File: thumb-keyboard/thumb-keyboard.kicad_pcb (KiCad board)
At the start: 2 copper layers, 120 x 60 mm, 128 parts, among them J1 Conn_01x02_Socket, U1 nice_nano

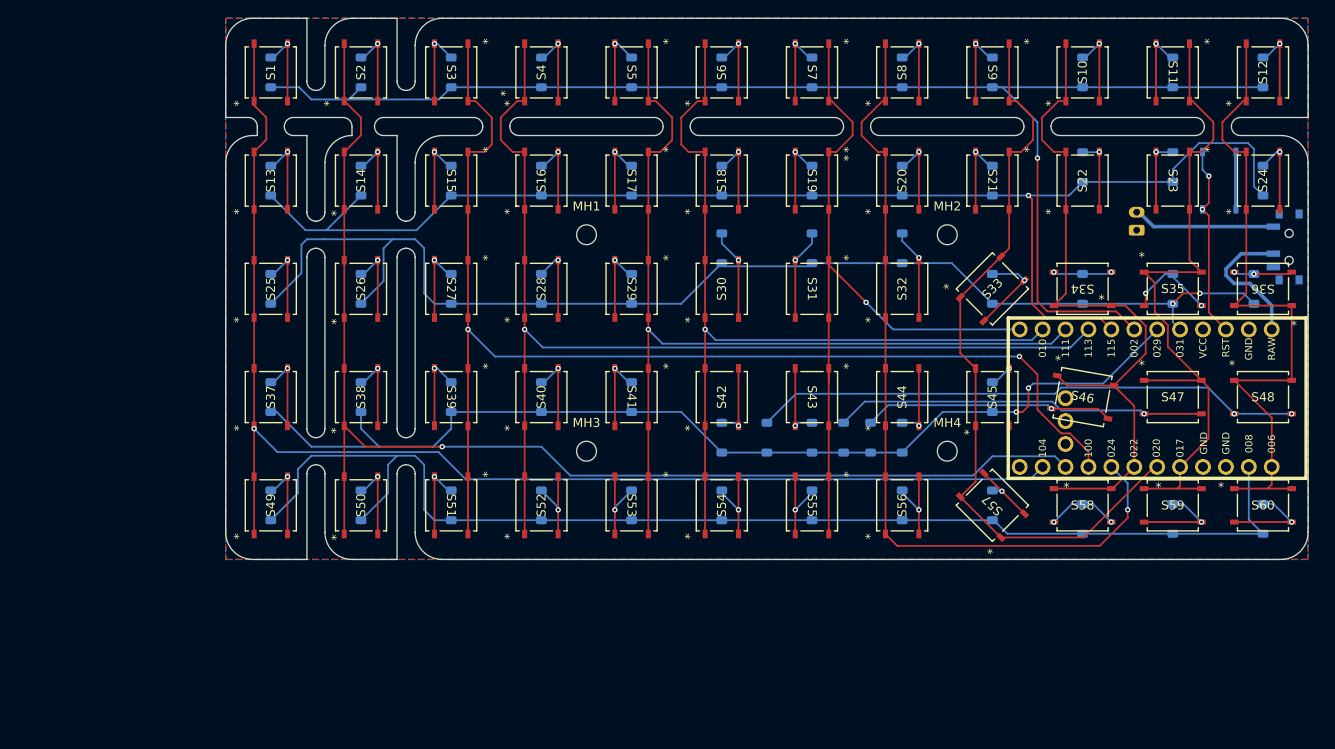
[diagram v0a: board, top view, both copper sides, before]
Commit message: going to try reducing the slot diam
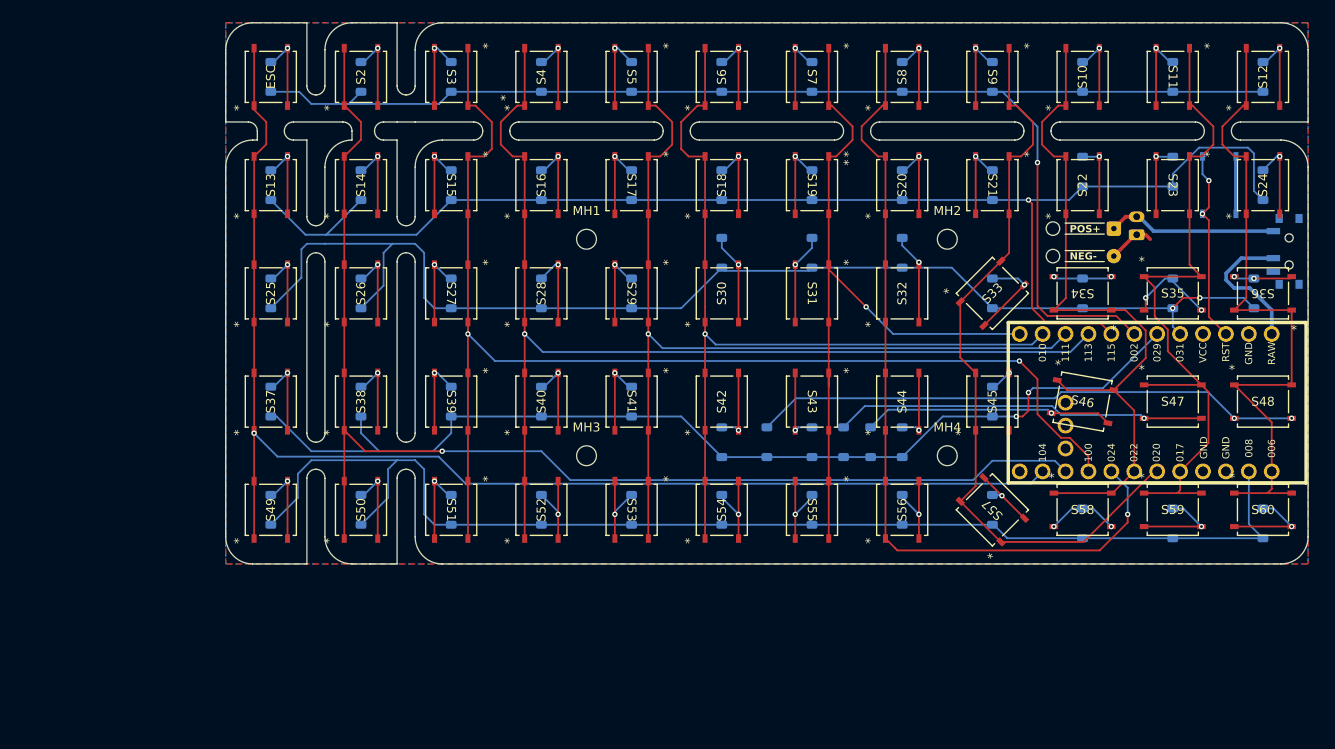
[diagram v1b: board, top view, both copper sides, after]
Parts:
- added GND - POS: SolderWire-0.1sqmm_1x02_P3.6mm_D0.4mm_OD1mm_Relief, Connector_Wire:SolderWire-0.1sqmm_1x02_P3.6mm_D0.4mm_OD1mm_Relief, F.Cu at (178.5, 70.6)
- S1: value PTS526 SK15 SMTR2 LFS -> ESC
- moved D1 0.50 mm to (85.0, 54.0)
- moved D10 0.50 mm to (175.0, 54.0)
- moved D11 0.50 mm to (185.0, 54.0)
- moved D12 0.50 mm to (195.0, 54.0)
- moved D13 0.50 mm to (85.0, 66.0)
- moved D14 0.50 mm to (95.0, 66.0)
- moved D15 0.50 mm to (105.0, 66.0)
- moved D16 0.50 mm to (115.0, 66.0)
- moved D17 0.50 mm to (125.0, 66.0)
- moved D18 0.50 mm to (135.0, 66.0)
- moved D19 0.50 mm to (145.0, 66.0)
- moved D2 0.50 mm to (95.0, 54.0)
- moved D20 0.50 mm to (155.0, 66.0)
- moved D21 0.50 mm to (165.0, 66.0)
- moved D22 0.50 mm to (175.0, 64.5)
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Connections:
- S62 pad SH1: /GND -> (no net)
- S62 pad SH2: /GND -> (no net)
- S62 pad SH3: /GND -> (no net)
- S62 pad SH4: /GND -> (no net)
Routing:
- net /GND: track 6.36 -> 11.6 mm
- net /BATP: track 15.8 -> 18.9 mm
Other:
- board text added: "NEG-"
- board text added: "POS+"

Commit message: Added ws2812b leds to thumb keyboard. they may be too tall. I may have to switch to the 222AMVBAR tactile switches and space everything out like a centimeter more. that would be a lot of work but would open up for other types of switches
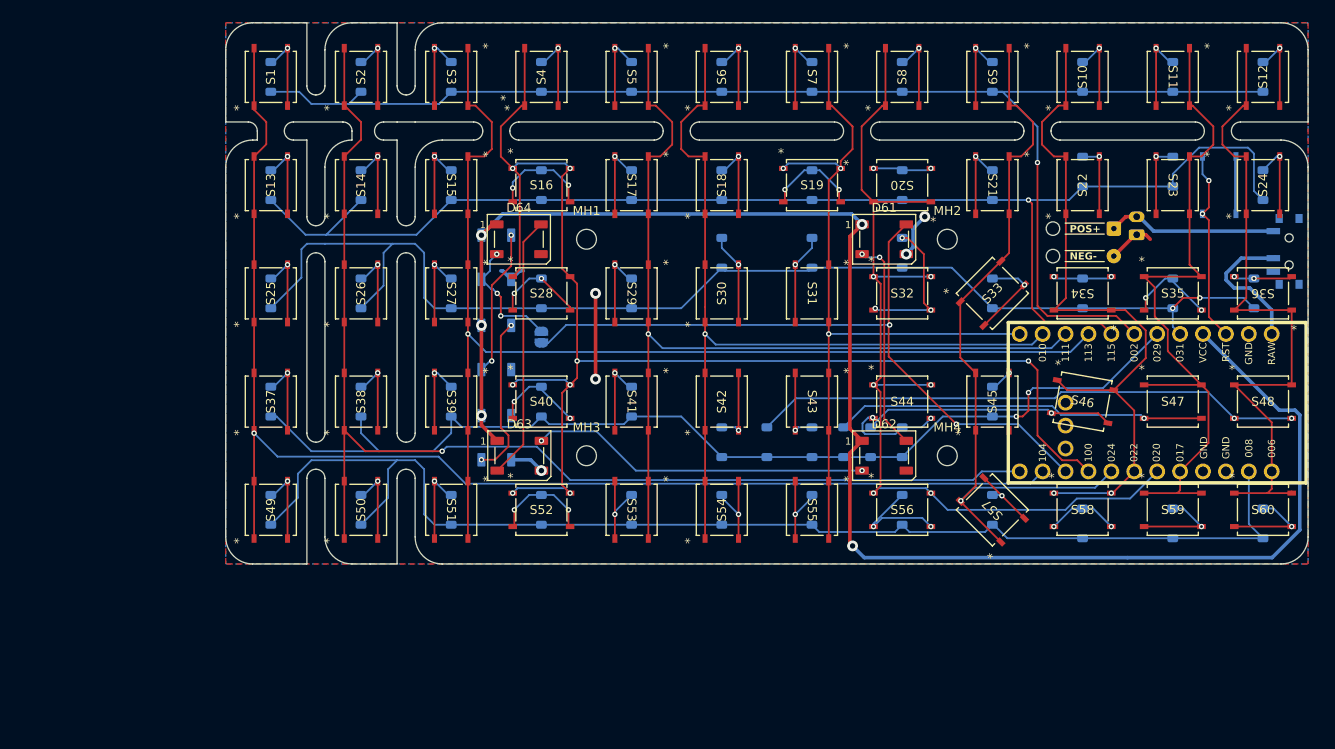
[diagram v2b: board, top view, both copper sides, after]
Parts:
- added D61: WS2812B, LED_SMD:LED_WS2812B_PLCC4_5.0x5.0mm_P3.2mm, F.Cu at (153.0, 72.0)
- added D62: WS2812B, LED_SMD:LED_WS2812B_PLCC4_5.0x5.0mm_P3.2mm, F.Cu at (153.0, 96.0)
- added D63: WS2812B, LED_SMD:LED_WS2812B_PLCC4_5.0x5.0mm_P3.2mm, F.Cu at (112.5, 96.0)
- added D64: WS2812B, LED_SMD:LED_WS2812B_PLCC4_5.0x5.0mm_P3.2mm, F.Cu at (112.5, 72.0)
- added D65: WS2812B, LED_SMD:LED_WS2812B_PLCC4_5.0x5.0mm_P3.2mm, B.Cu at (110.0, 74.0)
- added D66: WS2812B, LED_SMD:LED_WS2812B_PLCC4_5.0x5.0mm_P3.2mm, B.Cu at (110.0, 84.0)
- added D67: WS2812B, LED_SMD:LED_WS2812B_PLCC4_5.0x5.0mm_P3.2mm, B.Cu at (110.0, 94.0)
- added JumpIfNoFrontLED: SolderJumper-2_P1.3mm_Open_RoundedPad1.0x1.5mm, Jumper:SolderJumper-2_P1.3mm_Open_RoundedPad1.0x1.5mm, B.Cu at (115.0, 82.8)
- S1, S10, S11, S12, S13, S14, S15, S16, S17, S18, S19, S2, S20, S21, S22, S23, S24, S25, S26, S27, S28, S29, S3, S30, S31, S32, S33, S34, S35, S36, S37, S38, S39, S4, S40, S41, S42, S43, S44, S45, S46, S47, S48, S49, S5, S50, S51, S52, S53, S54, S55, S56, S57, S58, S59, S6, S60, S61, S7, S8, S9: footprint footprints:SMT_FS -> lowproswitch:SMT_FS
- turned S16 to 0 degrees
- turned S19 to 0 degrees
- turned S20 to 180 degrees
- turned S28 to 0 degrees
- turned S32 to 0 degrees
- turned S40 to 0 degrees
- turned S44 to 0 degrees
- turned S52 to 0 degrees
- turned S56 to 0 degrees
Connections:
- net Net-(D1-A) renamed /C0R0D
- U1 pad 10: /COL1 -> /RGBDIN
- U1 pad 12: unconnected-(U1-P1.06-Pad12) -> /COL1
- U1 pad 16: /COL3 -> /COL2
- U1 pad 21: unconnected-(U1-VCC-Pad21) -> /VCC
- U1 pad 6: /COL8 -> /COL7
- U1 pad 8: /COL7 -> /COL8
- U1 pad 9: /COL2 -> /COL3
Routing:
- net /VCC: track 0.00 -> 185.6 mm, vias 0 -> 5
- net /RGBDIN: track 0.00 -> 79.8 mm, vias 0 -> 2
- net Net-(D62-DOUT): track 0.00 -> 37.8 mm, vias 0 -> 2
- net /COL3: track 122.0 -> 152.4 mm, vias 1 -> 8
- net Net-(D63-DOUT): track 0.00 -> 29.3 mm
- net Net-(D61-DOUT): track 0.00 -> 23.7 mm, vias 0 -> 2
- net /GND: track 11.6 -> 33.2 mm, vias 0 -> 5
- net Net-(D66-DOUT): track 0.00 -> 17.9 mm, vias 0 -> 2
- net Net-(D65-DOUT): track 0.00 -> 16.4 mm, vias 0 -> 2
- net Net-(D64-DOUT): track 0.00 -> 13.8 mm, vias 0 -> 3
- net /COL7: track 92.3 -> 106.0 mm, vias 1 -> 6
- net /COL2: track 136.5 -> 128.6 mm, vias 2 -> 1
- net Net-(D32-A): track 9.83 -> 15.9 mm, vias 1 -> 3
- net /COL1: track 139.5 -> 133.9 mm
- net Net-(D56-A): track 9.28 -> 12.3 mm, vias 1 -> 2
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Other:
- board text added: "301230 battery"

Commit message: working on different switches. last commit before adding the B3F-1000 switch option and extending the x gap from 10 - 12 mm
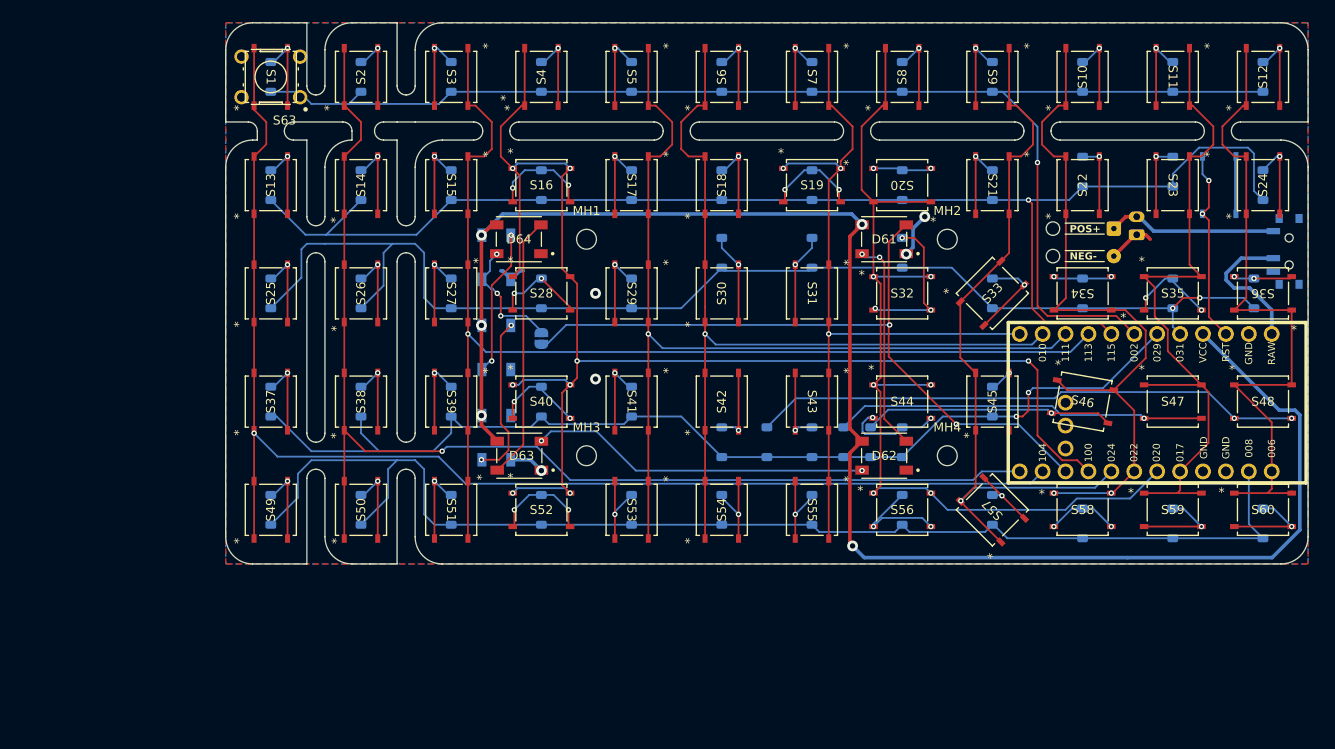
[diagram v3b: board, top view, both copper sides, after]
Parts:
- added S63: B3F-1000, B3F_1000:SW_B3F-1000, F.Cu at (85.0, 54.0)
- D61, D62, D63, D64, D65, D66, D67: footprint LED_SMD:LED_WS2812B_PLCC4_5.0x5.0mm_P3.2mm -> 1655:LED_1655
- moved JumpIfNoFrontLED 0.15 mm to (115.0, 83.0)
- turned D61 to 180 degrees
- turned D62 to 180 degrees
- turned D63 to 180 degrees
- turned D64 to 180 degrees
- turned D65 to 90 degrees
- turned D66 to 90 degrees
- turned D67 to 90 degrees
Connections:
- D61 pad 1: /VCC -> /GND
- D61 pad 2: Net-(D61-DOUT) -> /RGBDIN
- D61 pad 3: /GND -> /VCC
- D61 pad 4: /RGBDIN -> Net-(D61-DOUT)
- D62 pad 1: /VCC -> /GND
- D62 pad 2: Net-(D62-DOUT) -> Net-(D61-DOUT)
- D62 pad 3: /GND -> /VCC
- D62 pad 4: Net-(D61-DOUT) -> Net-(D62-DOUT)
- D63 pad 1: /VCC -> /GND
- D63 pad 2: Net-(D63-DOUT) -> Net-(D62-DOUT)
- D63 pad 3: /GND -> /VCC
- D63 pad 4: Net-(D62-DOUT) -> Net-(D63-DOUT)
- D64 pad 1: /VCC -> /GND
- D64 pad 2: Net-(D64-DOUT) -> Net-(D63-DOUT)
- D64 pad 3: /GND -> /VCC
- D64 pad 4: Net-(D63-DOUT) -> Net-(D64-DOUT)
- D65 pad 1: /VCC -> /GND
- D65 pad 2: Net-(D65-DOUT) -> Net-(D64-DOUT)
- D65 pad 3: /GND -> /VCC
- D65 pad 4: Net-(D64-DOUT) -> Net-(D65-DOUT)
- D66 pad 1: /VCC -> /GND
- D66 pad 2: Net-(D66-DOUT) -> Net-(D65-DOUT)
- D66 pad 3: /GND -> /VCC
- D66 pad 4: Net-(D65-DOUT) -> Net-(D66-DOUT)
- D67 pad 1: /VCC -> /GND
- D67 pad 2: unconnected-(D67-DOUT-Pad2) -> Net-(D66-DOUT)
- D67 pad 3: /GND -> /VCC
- D67 pad 4: Net-(D66-DOUT) -> unconnected-(D67-DOUT-Pad4)
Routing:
- net /GND: track 33.2 -> 23.7 mm

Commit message: first commit after change to branch with optional B3F-1000 switches. footprint is going to be 144x60
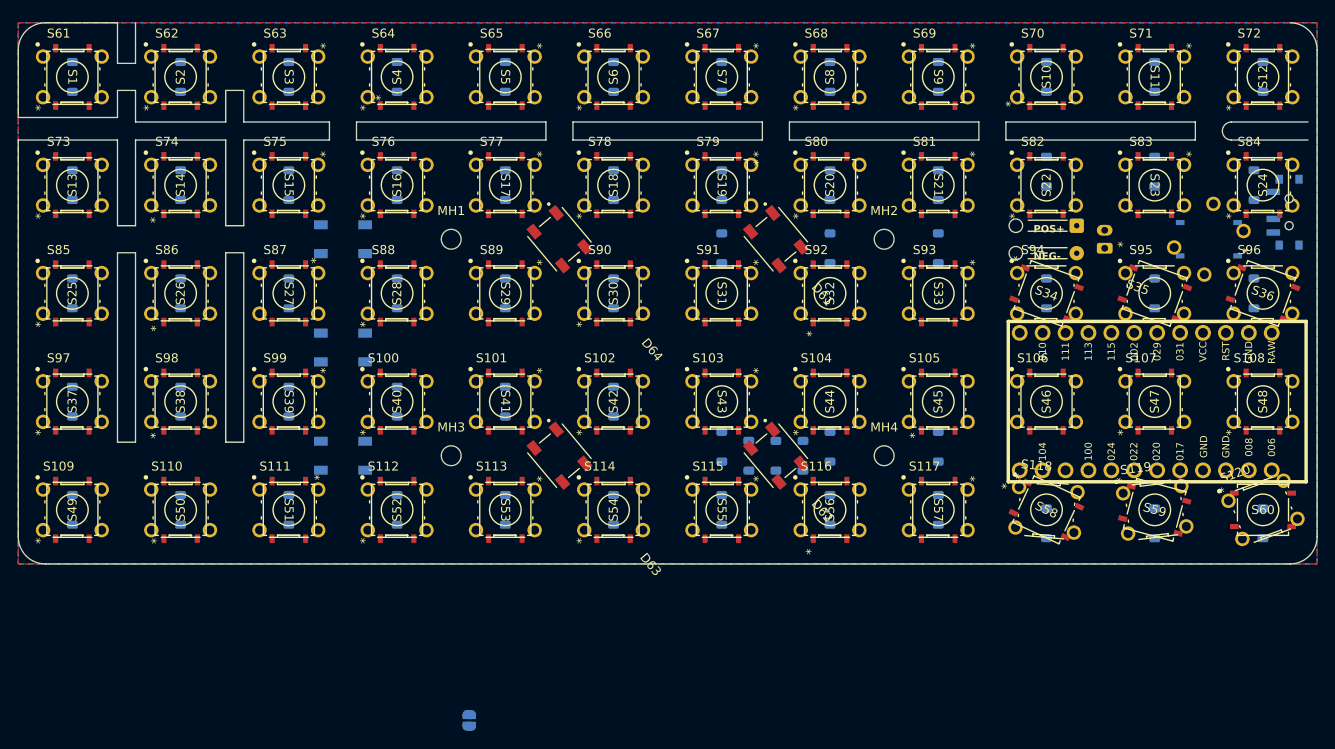
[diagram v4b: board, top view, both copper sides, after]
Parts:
- added S100: B3F-1000, B3F_1000:SW_B3F-1000, F.Cu at (99.0, 90.0)
- added S101: B3F-1000, B3F_1000:SW_B3F-1000, F.Cu at (111.0, 90.0)
- added S102: B3F-1000, B3F_1000:SW_B3F-1000, F.Cu at (123.0, 90.0)
- added S103: B3F-1000, B3F_1000:SW_B3F-1000, F.Cu at (135.0, 90.0)
- added S104: B3F-1000, B3F_1000:SW_B3F-1000, F.Cu at (147.0, 90.0)
- added S105: B3F-1000, B3F_1000:SW_B3F-1000, F.Cu at (159.0, 90.0)
- added S106: B3F-1000, B3F_1000:SW_B3F-1000, F.Cu at (171.0, 90.0)
- added S107: B3F-1000, B3F_1000:SW_B3F-1000, F.Cu at (183.0, 90.0)
- added S108: B3F-1000, B3F_1000:SW_B3F-1000, F.Cu at (195.0, 90.0)
- added S109: B3F-1000, B3F_1000:SW_B3F-1000, F.Cu at (63.0, 102.0)
- added S110: B3F-1000, B3F_1000:SW_B3F-1000, F.Cu at (75.0, 102.0)
- added S111: B3F-1000, B3F_1000:SW_B3F-1000, F.Cu at (87.0, 102.0)
- added S112: B3F-1000, B3F_1000:SW_B3F-1000, F.Cu at (99.0, 102.0)
- added S113: B3F-1000, B3F_1000:SW_B3F-1000, F.Cu at (111.0, 102.0)
- added S114: B3F-1000, B3F_1000:SW_B3F-1000, F.Cu at (123.0, 102.0)
- added S115: B3F-1000, B3F_1000:SW_B3F-1000, F.Cu at (135.0, 102.0)
- added S116: B3F-1000, B3F_1000:SW_B3F-1000, F.Cu at (147.0, 102.0)
- added S117: B3F-1000, B3F_1000:SW_B3F-1000, F.Cu at (159.0, 102.0)
- added S118: B3F-1000, B3F_1000:SW_B3F-1000, F.Cu at (171.0, 102.0)
- added S119: B3F-1000, B3F_1000:SW_B3F-1000, F.Cu at (183.0, 102.0)
- added S120: B3F-1000, B3F_1000:SW_B3F-1000, F.Cu at (195.0, 102.0)
- added S123: B3F-1000, B3F_1000:SW_B3F-1000, B.Cu at (189.0, 72.0)
- added S61: B3F-1000, B3F_1000:SW_B3F-1000, F.Cu at (63.0, 54.0)
- added S62: B3F-1000, B3F_1000:SW_B3F-1000, F.Cu at (75.0, 54.0)
- added S64: B3F-1000, B3F_1000:SW_B3F-1000, F.Cu at (99.0, 54.0)
- added S65: B3F-1000, B3F_1000:SW_B3F-1000, F.Cu at (111.0, 54.0)
- added S66: B3F-1000, B3F_1000:SW_B3F-1000, F.Cu at (123.0, 54.0)
- added S67: B3F-1000, B3F_1000:SW_B3F-1000, F.Cu at (135.0, 54.0)
- added S68: B3F-1000, B3F_1000:SW_B3F-1000, F.Cu at (147.0, 54.0)
- added S69: B3F-1000, B3F_1000:SW_B3F-1000, F.Cu at (159.0, 54.0)
- added S70: B3F-1000, B3F_1000:SW_B3F-1000, F.Cu at (171.0, 54.0)
- added S71: B3F-1000, B3F_1000:SW_B3F-1000, F.Cu at (183.0, 54.0)
- added S72: B3F-1000, B3F_1000:SW_B3F-1000, F.Cu at (195.0, 54.0)
- added S73: B3F-1000, B3F_1000:SW_B3F-1000, F.Cu at (63.0, 66.0)
- added S74: B3F-1000, B3F_1000:SW_B3F-1000, F.Cu at (75.0, 66.0)
- added S75: B3F-1000, B3F_1000:SW_B3F-1000, F.Cu at (87.0, 66.0)
- added S76: B3F-1000, B3F_1000:SW_B3F-1000, F.Cu at (99.0, 66.0)
- added S77: B3F-1000, B3F_1000:SW_B3F-1000, F.Cu at (111.0, 66.0)
- added S78: B3F-1000, B3F_1000:SW_B3F-1000, F.Cu at (123.0, 66.0)
- added S79: B3F-1000, B3F_1000:SW_B3F-1000, F.Cu at (135.0, 66.0)
- added S80: B3F-1000, B3F_1000:SW_B3F-1000, F.Cu at (147.0, 66.0)
- added S81: B3F-1000, B3F_1000:SW_B3F-1000, F.Cu at (159.0, 66.0)
- added S82: B3F-1000, B3F_1000:SW_B3F-1000, F.Cu at (171.0, 66.0)
- added S83: B3F-1000, B3F_1000:SW_B3F-1000, F.Cu at (183.0, 66.0)
- added S84: B3F-1000, B3F_1000:SW_B3F-1000, F.Cu at (195.0, 66.0)
- added S85: B3F-1000, B3F_1000:SW_B3F-1000, F.Cu at (63.0, 78.0)
- added S86: B3F-1000, B3F_1000:SW_B3F-1000, F.Cu at (75.0, 78.0)
- added S87: B3F-1000, B3F_1000:SW_B3F-1000, F.Cu at (87.0, 78.0)
- added S88: B3F-1000, B3F_1000:SW_B3F-1000, F.Cu at (99.0, 78.0)
- added S89: B3F-1000, B3F_1000:SW_B3F-1000, F.Cu at (111.0, 78.0)
- added S90: B3F-1000, B3F_1000:SW_B3F-1000, F.Cu at (123.0, 78.0)
- added S91: B3F-1000, B3F_1000:SW_B3F-1000, F.Cu at (135.0, 78.0)
- added S92: B3F-1000, B3F_1000:SW_B3F-1000, F.Cu at (147.0, 78.0)
- added S93: B3F-1000, B3F_1000:SW_B3F-1000, F.Cu at (159.0, 78.0)
- added S94: B3F-1000, B3F_1000:SW_B3F-1000, F.Cu at (171.0, 78.0)
- added S95: B3F-1000, B3F_1000:SW_B3F-1000, F.Cu at (183.0, 78.0)
- added S96: B3F-1000, B3F_1000:SW_B3F-1000, F.Cu at (195.0, 78.0)
- added S97: B3F-1000, B3F_1000:SW_B3F-1000, F.Cu at (63.0, 90.0)
- added S98: B3F-1000, B3F_1000:SW_B3F-1000, F.Cu at (75.0, 90.0)
- added S99: B3F-1000, B3F_1000:SW_B3F-1000, F.Cu at (87.0, 90.0)
- moved JumpIfNoFrontLED 43.1 mm to (107.0, 125.3)
- moved D1 22.0 mm to (63.0, 54.0)
- moved D13 22.0 mm to (63.0, 66.0)
- moved D25 22.0 mm to (63.0, 78.0)
- moved D37 22.0 mm to (63.0, 90.0)
- moved D49 22.0 mm to (63.0, 102.0)
- moved S1 22.0 mm to (63.0, 54.0)
- moved S13 22.0 mm to (63.0, 66.0)
- moved S25 22.0 mm to (63.0, 78.0)
- moved S37 22.0 mm to (63.0, 90.0)
- moved S49 22.0 mm to (63.0, 102.0)
- moved D14 20.0 mm to (75.0, 66.0)
- moved D2 20.0 mm to (75.0, 54.0)
- moved D26 20.0 mm to (75.0, 78.0)
- moved D38 20.0 mm to (75.0, 90.0)
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- renumbered S62 to S121, S61 to S122
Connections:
- net Net-(D10-A) renamed /C9R0D
- net Net-(D11-A) renamed /C10R0D
- net Net-(D12-A) renamed /C11R0D
- net Net-(D13-A) renamed /C0R1D
- net Net-(D14-A) renamed /C1R1D
- net Net-(D15-A) renamed /C2R1D
- net Net-(D16-A) renamed /C3R1D
- net Net-(D17-A) renamed /C4R1D
- net Net-(D18-A) renamed /C5R1D
- net Net-(D19-A) renamed /C6R1D
- net Net-(D2-A) renamed /C1R0D
- net Net-(D20-A) renamed /C7R1D
- net Net-(D21-A) renamed /C8R1D
- net Net-(D22-A) renamed /C9R1D
- net Net-(D23-A) renamed /C10R1D
- net Net-(D24-A) renamed /C11R1D
- net Net-(D25-A) renamed /C0R2D
- net Net-(D26-A) renamed /C1R2D
- net Net-(D27-A) renamed /C2R2D
- net Net-(D28-A) renamed /C3R2D
- net Net-(D29-A) renamed /C4R2D
- net Net-(D30-A) renamed /C5R2D
- net Net-(D31-A) renamed /C6R2D
- net Net-(D32-A) renamed /C7R2D
- net Net-(D33-A) renamed /C8R2D
- net Net-(D34-A) renamed /C9R2D
- net Net-(D35-A) renamed /C10R2D
- net Net-(D36-A) renamed /C11R2D
- net Net-(D37-A) renamed /C0R3D
- net Net-(D38-A) renamed /C1R3D
- net Net-(D39-A) renamed /C2R3D
- net Net-(D4-A) renamed /C3R0D
- net Net-(D40-A) renamed /C3R3D
- net Net-(D41-A) renamed /C4R3D
- net Net-(D42-A) renamed /C5R3D
- net Net-(D43-A) renamed /C6R3D
- net Net-(D44-A) renamed /C7R3D
- net Net-(D45-A) renamed /C8R3D
- net Net-(D46-A) renamed /C9R3D
- net Net-(D47-A) renamed /C10R3D
- net Net-(D48-A) renamed /C11R3D
- net Net-(D49-A) renamed /C0R4D
- net Net-(D5-A) renamed /C4R0D
- net Net-(D50-A) renamed /C1R4D
- net Net-(D51-A) renamed /C2R4D
- net Net-(D52-A) renamed /C3R4D
- net Net-(D53-A) renamed /C4R4D
- net Net-(D54-A) renamed /C5R4D
- net Net-(D55-A) renamed /C6R4D
- net Net-(D56-A) renamed /C7R4D
- net Net-(D57-A) renamed /C8R4D
- net Net-(D58-A) renamed /C9R4D
- net Net-(D59-A) renamed /C10R4D
- net Net-(D6-A) renamed /C5R0D
- net Net-(D60-A) renamed /C11R4D
- net Net-(D7-A) renamed /C6R0D
- net Net-(D8-A) renamed /C7R0D
- net Net-(D9-A) renamed /C8R0D
- D3 pad 2: Net-(D3-A) -> /C2R0D
- S3 pad 3: Net-(D3-A) -> /C2R0D
- S3 pad 4: Net-(D3-A) -> /C2R0D
- S63 pad 1: /C0R0D -> /COL2
- S63 pad 2: /C0R0D -> /COL2
- S63 pad 3: /COL0 -> /C2R0D
- S63 pad 4: /COL0 -> /C2R0D
- U1 pad 12: /COL1 -> /COL9
- U1 pad 20: /ROW2 -> /COL10
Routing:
- net /VCC: track 185.6 -> 0.00 mm, vias 5 -> 0
- net /COL3: track 152.4 -> 0.00 mm, vias 8 -> 0
- net /ROW0: track 151.5 -> 0.00 mm, vias 1 -> 0
- net /ROW1: track 148.8 -> 0.00 mm, vias 1 -> 0
- net /COL0: track 145.8 -> 0.00 mm, vias 1 -> 0
- net /ROW4: track 139.2 -> 0.00 mm
- net /ROW2: track 136.5 -> 0.00 mm, vias 2 -> 0
- net /COL1: track 133.9 -> 0.00 mm, vias 1 -> 0
- net /COL2: track 128.6 -> 0.00 mm, vias 1 -> 0
- net /ROW3: track 117.8 -> 0.00 mm, vias 2 -> 0
- net /COL7: track 106.0 -> 0.00 mm, vias 6 -> 0
- net /COL4: track 105.4 -> 0.00 mm, vias 1 -> 0
- net /COL5: track 96.5 -> 0.00 mm, vias 1 -> 0
- net /COL6: track 84.7 -> 0.00 mm, vias 3 -> 0
- net /COL8: track 81.8 -> 0.00 mm, vias 1 -> 0
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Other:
- board size 120 x 60 mm -> 144 x 60 mm
